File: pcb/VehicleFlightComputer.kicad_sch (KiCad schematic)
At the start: 52 parts, among them J3 USB_C_Receptacle, J4 Debug, Q1 S8050, SW1 B3U-1000P, U1 STM32H533VET6, U2 LIS2MDL, U3 LSM6DSV32X, U4 MCP2221A-I/ST, U5 AP2112K-3.3

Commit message: Added vehicle PDS I/O connector to `VehicleFlightComputer`.
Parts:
- added J1: FFC2B28-24-G, pcb:Flat Flexible Cable 24-Pin 0.5mm Connector, symbol Connector_Generic:Conn_01x22
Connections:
- net +3.3V: now also J1.12 (Pin_12), J1.18 (Pin_18), J1.5 (Pin_5)
- net GND: now also J1.1 (Pin_1), J1.11 (Pin_11), J1.13 (Pin_13), J1.15 (Pin_15), J1.22 (Pin_22), J1.9 (Pin_9)
- net sd_cmd: no longer names the net of U1.83 (PD2)
- net sd_data_0: no longer names the net of U1.65 (PC8)
- net sd_data_1: no longer names the net of U1.66 (PC9)
- net sd_data_2: no longer names the net of U1.78 (PC10)
- net sd_data_3: no longer names the net of U1.79 (PC11)
- new net +5V: J1.10 (Pin_10), J1.14 (Pin_14)
- new net BATTERY_ALLOWED: J1.17 (Pin_17)
- new net EXTERNAL_DETECTED: J1.16 (Pin_16)
- new net MOTOR_DIR_X: J1.21 (Pin_21)
- new net MOTOR_DIR_Y: J1.20 (Pin_20)
- new net MOTOR_DIR_Z: J1.19 (Pin_19)
- new net MOTOR_DISABLE: J1.6 (Pin_6)
- new net MOTOR_STEP_X: J1.2 (Pin_2)
- new net MOTOR_STEP_Y: J1.3 (Pin_3)
- new net MOTOR_STEP_Z: J1.4 (Pin_4)
- new net MOTOR_UART_RX: J1.7 (Pin_7)
- new net MOTOR_UART_TX: J1.8 (Pin_8)
- no-connect marks 135 -> 140
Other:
- removed sheet uSD Connector
- note added: "Pin ordering should account for backwards connection."
- note added: "Vehicle PDS I/O (V0)."
- moved on the sheet: BZ1, BZ2, C1, C10, C11, C12, C13, C15, C2, C3, C4, C5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

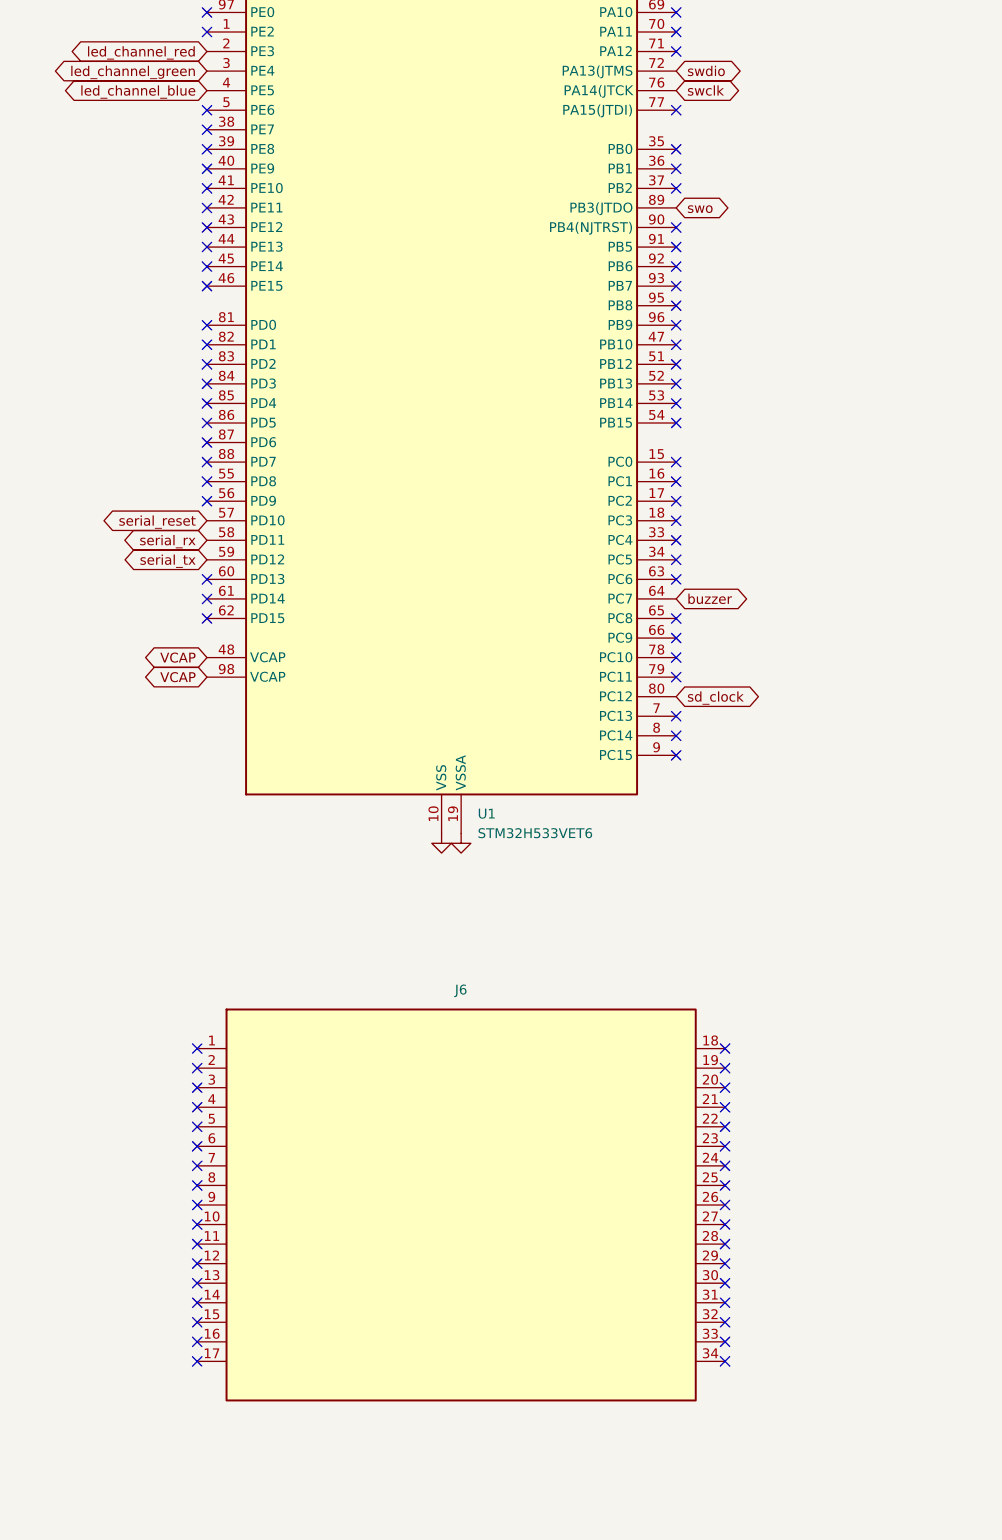
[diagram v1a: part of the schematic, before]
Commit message: Updated `VehicleStackConnector` with pin usages.
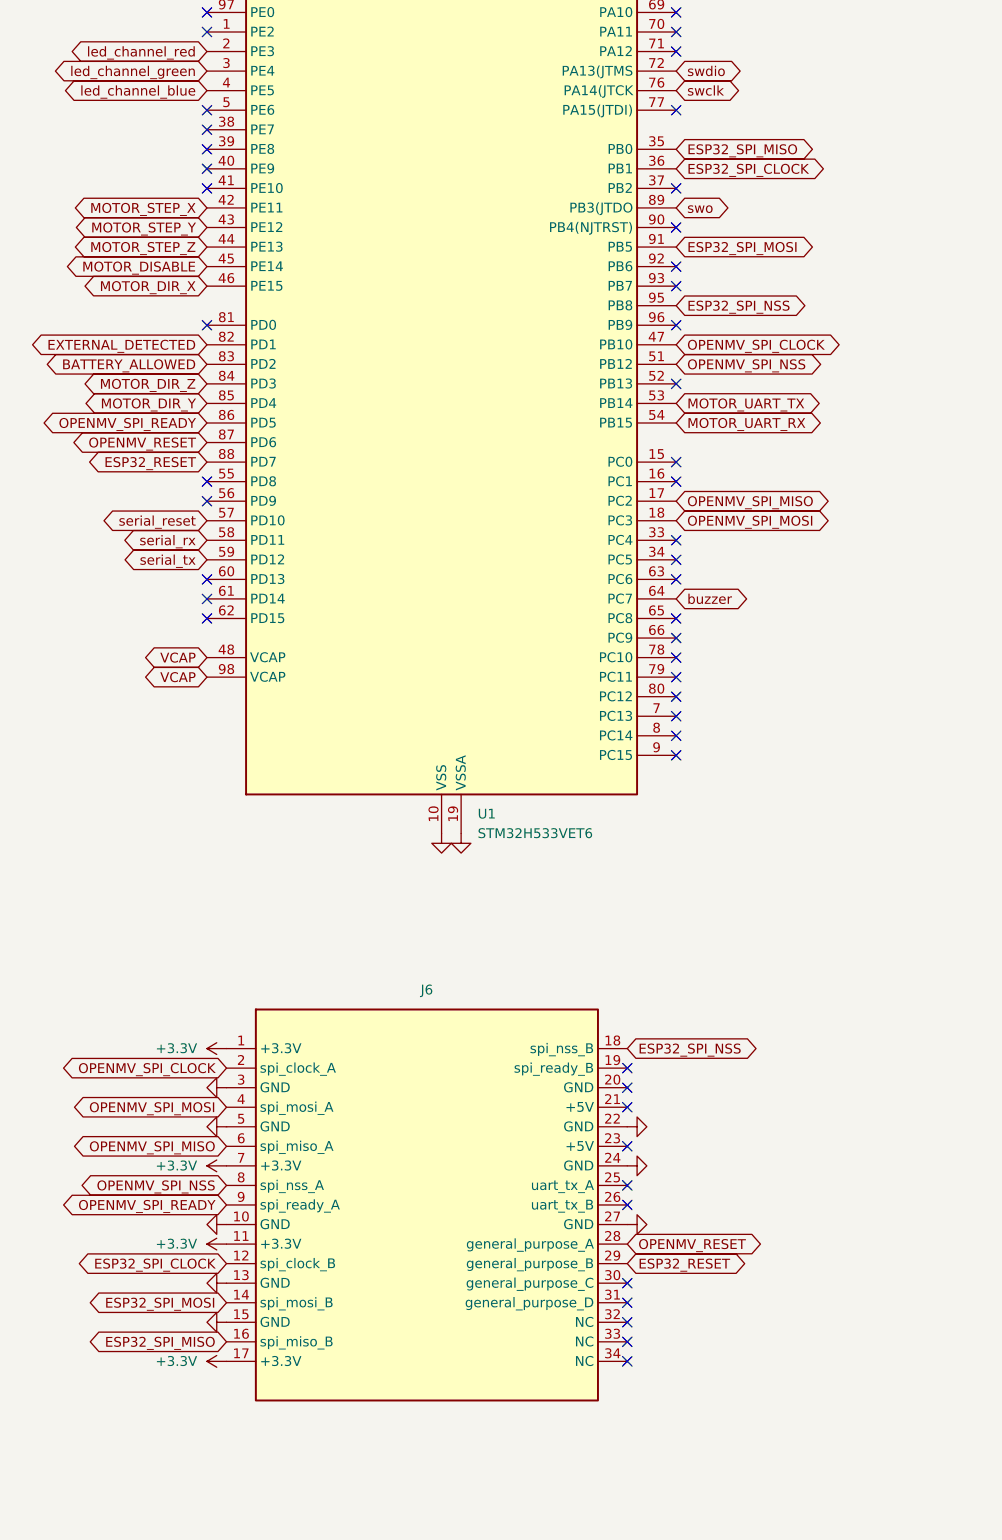
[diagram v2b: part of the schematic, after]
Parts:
- Q1: footprint Package_TO_SOT_SMD:SOT-23_Handsoldering -> Package_TO_SOT_THT:TO-92_Inline
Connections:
- net +3.3V: now also J6.1 (+3.3V), J6.11 (+3.3V), J6.17 (+3.3V), J6.7 (+3.3V)
- net BATTERY_ALLOWED: now also U1.83 (PD2)
- net EXTERNAL_DETECTED: now also U1.82 (PD1)
- net GND: now also J6.10 (GND), J6.13 (GND), J6.15 (GND), J6.22 (GND), J6.24 (GND), J6.27 (GND), J6.3 (GND), J6.5 (GND)
- net MOTOR_DIR_X: now also U1.46 (PE15)
- net MOTOR_DIR_Y: now also U1.85 (PD4)
- net MOTOR_DIR_Z: now also U1.84 (PD3)
- net MOTOR_DISABLE: now also U1.45 (PE14)
- net MOTOR_STEP_X: now also U1.42 (PE11)
- net MOTOR_STEP_Y: now also U1.43 (PE12)
- net MOTOR_STEP_Z: now also U1.44 (PE13)
- net MOTOR_UART_RX: now also U1.54 (PB15)
- net MOTOR_UART_TX: now also U1.53 (PB14)
- net ESP32_SPI_CLOCK: now reaches J6.12 (spi_clock_B)
- net ESP32_SPI_CLOCK: now also U1.36 (PB1)
- net ESP32_SPI_MOSI: now reaches J6.14 (spi_mosi_B)
- net ESP32_SPI_MOSI: now also U1.91 (PB5)
- net ESP32_SPI_MISO: now reaches J6.16 (spi_miso_B)
- net ESP32_SPI_MISO: now also U1.35 (PB0)
- net ESP32_SPI_NSS: now reaches J6.18 (spi_nss_B)
- net ESP32_SPI_NSS: now also U1.95 (PB8)
- net OPENMV_SPI_CLOCK: now reaches J6.2 (spi_clock_A)
- net OPENMV_SPI_CLOCK: now also U1.47 (PB10)
- net OPENMV_RESET: now reaches J6.28 (general_purpose_A)
- net OPENMV_RESET: now also U1.87 (PD6)
- net ESP32_RESET: now reaches J6.29 (general_purpose_B)
- net ESP32_RESET: now also U1.88 (PD7)
- net OPENMV_SPI_MOSI: now reaches J6.4 (spi_mosi_A)
- net OPENMV_SPI_MOSI: now also U1.18 (PC3)
- net OPENMV_SPI_MISO: now reaches J6.6 (spi_miso_A)
- net OPENMV_SPI_MISO: now also U1.17 (PC2)
- net OPENMV_SPI_NSS: now reaches J6.8 (spi_nss_A)
- net OPENMV_SPI_NSS: now also U1.51 (PB12)
- net OPENMV_SPI_READY: now reaches J6.9 (spi_ready_A)
- net OPENMV_SPI_READY: now also U1.86 (PD5)
- net sd_clock: no longer names the net of U1.80 (PC12)
- no-connect marks 140 -> 96

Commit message: `Debug Buzzer (V5 : AST only).`
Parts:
- removed BZ2: WT-1205, Buzzer_Beeper:MagneticBuzzer_ProSignal_ABT-410-RC, symbol Device:Buzzer
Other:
- note added: "Debug Buzzer (V5 : AST only)."
- note removed: "Debug Buzzer (V4 : Transistor)."
- note removed: "TODO: The AST1109MLTRQ and WT-1205 buzzers have similar footprint area, but the former has a much smaller height. As precaution, we'll have a footprint for both buzzers in case we design for the AST1109MLTRQ wrong."
- moved on the sheet: BZ1, C1, C10, C2, C3, C4, C5, C6, C8, C9, H1, H2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

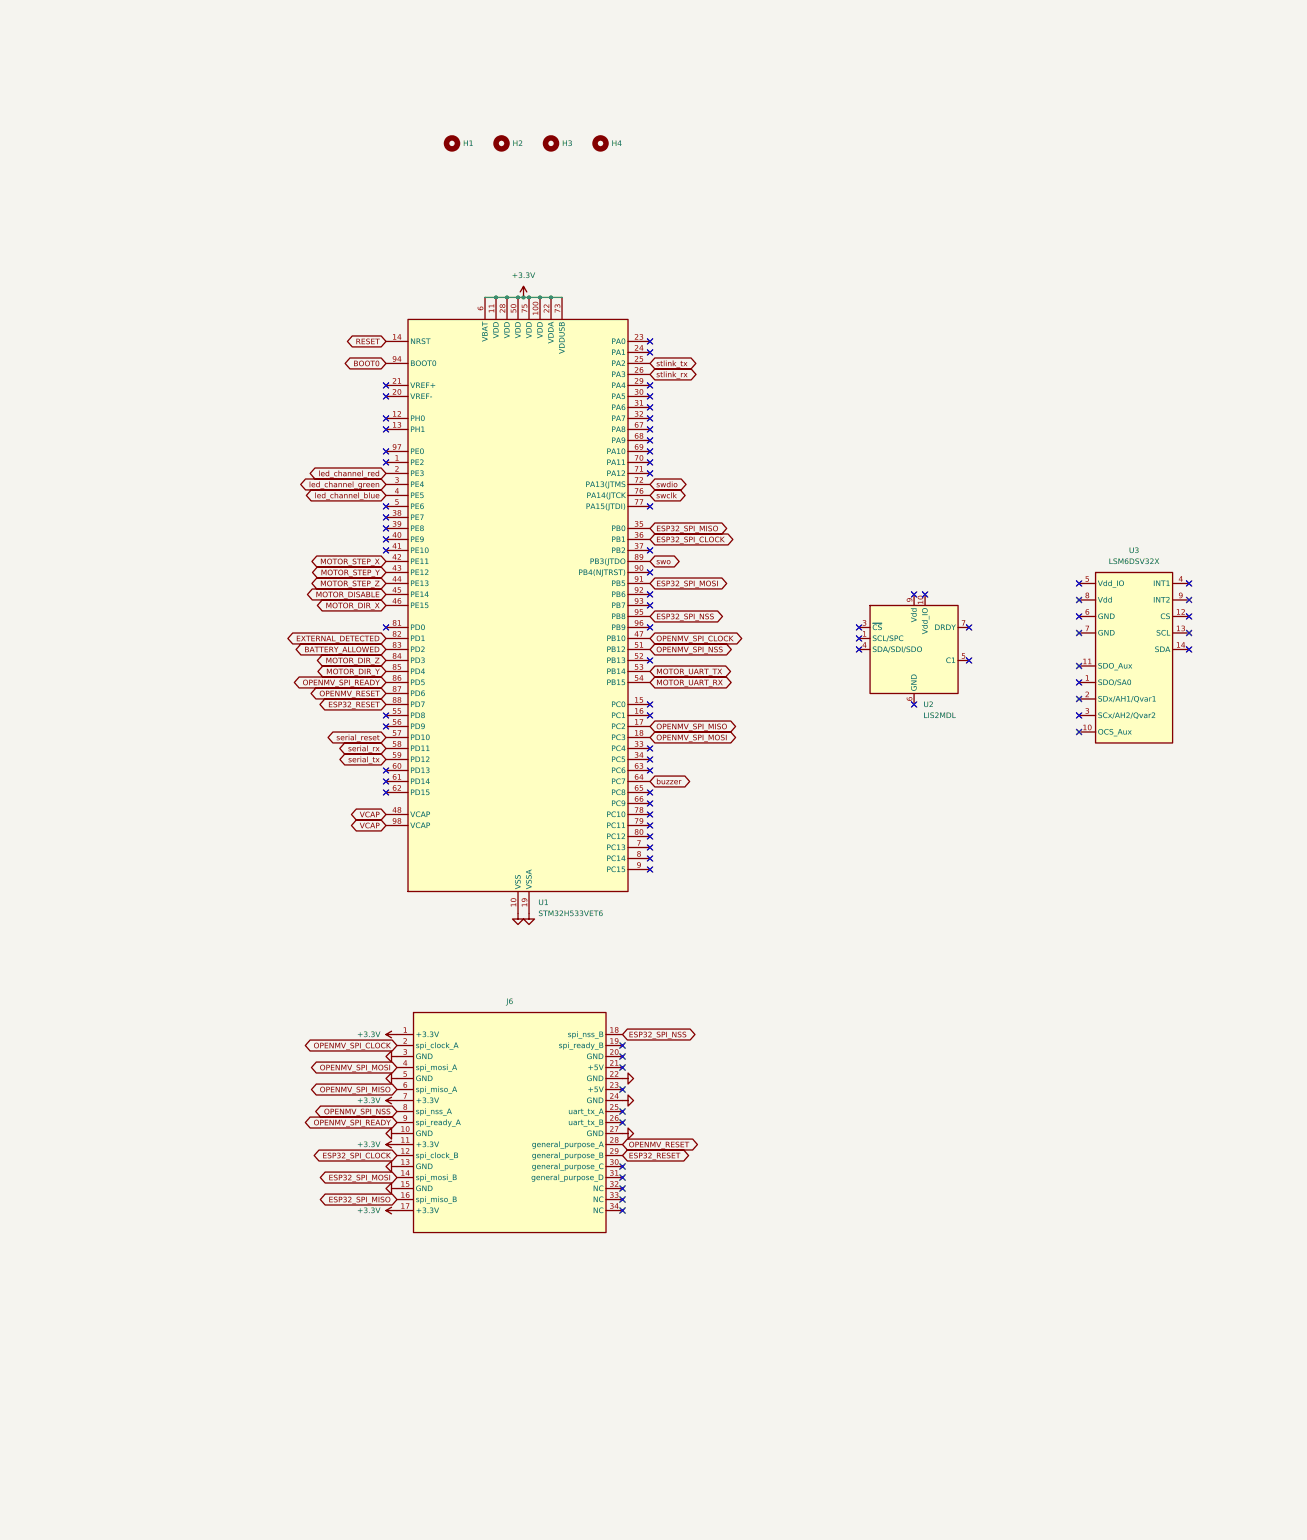
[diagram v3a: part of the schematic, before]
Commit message: Set up schematic for LSM6DSV32X on `VehicleFlightComputer`.
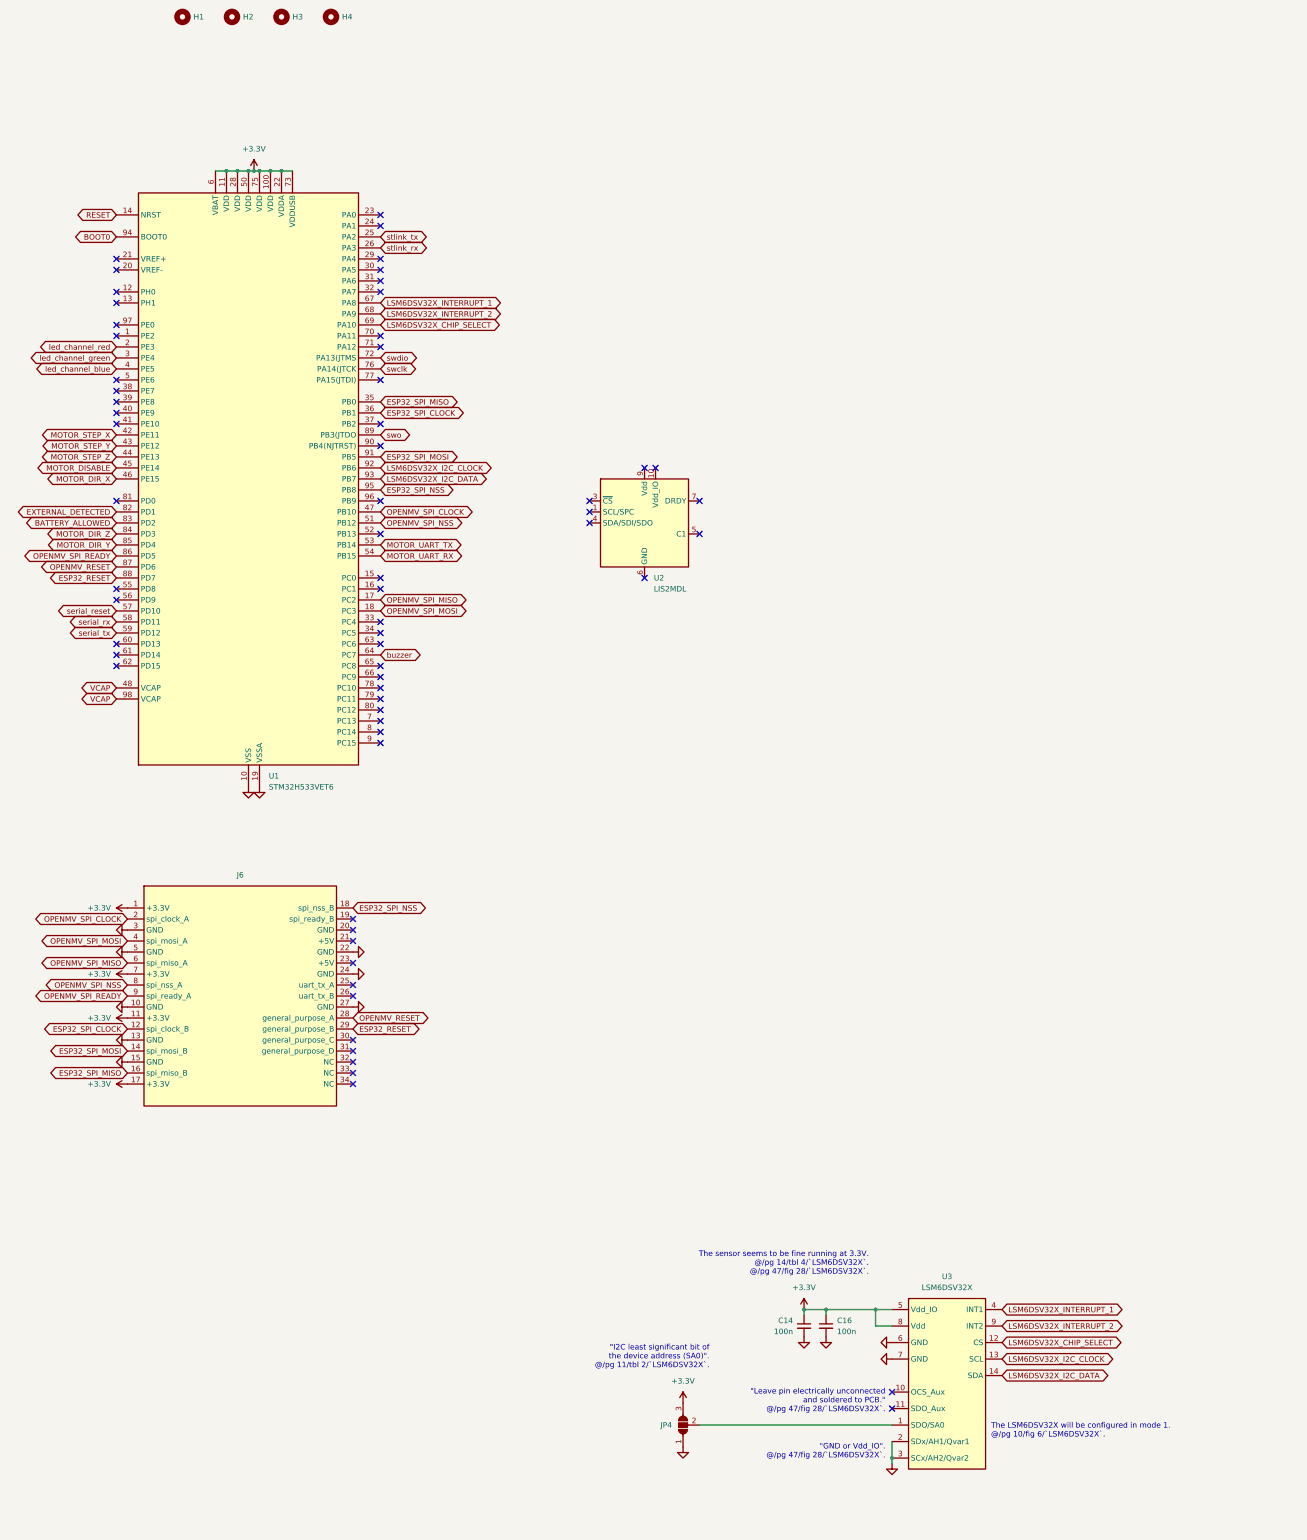
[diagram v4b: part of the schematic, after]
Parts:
- added C14, C16: 100n, Capacitor_SMD:C_1206_3216Metric_Pad1.33x1.80mm_HandSolder, symbol Device:C_Small
- added JP4: SolderJumper_3_Open, symbol Jumper:SolderJumper_3_Open
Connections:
- net +3.3V: now also U3.5 (Vdd_IO), U3.8 (Vdd), C14.1, C16.1, JP4.3 (B)
- net GND: now also U3.2 (SDx/AH1/Qvar1), U3.3 (SCx/AH2/Qvar2), U3.6 (GND), U3.7 (GND), C14.2, C16.2, JP4.1 (A)
- net at U3.1 (SDO/SA0): now also JP4.2 (C)
- net LSM6DSV32X_CHIP_SELECT: now reaches U3.12 (CS)
- net LSM6DSV32X_CHIP_SELECT: now also U1.69 (PA10)
- net LSM6DSV32X_I2C_CLOCK: now reaches U3.13 (SCL)
- net LSM6DSV32X_I2C_CLOCK: now also U1.92 (PB6)
- net LSM6DSV32X_I2C_DATA: now reaches U3.14 (SDA)
- net LSM6DSV32X_I2C_DATA: now also U1.93 (PB7)
- net LSM6DSV32X_INTERRUPT_1: now reaches U3.4 (INT1)
- net LSM6DSV32X_INTERRUPT_1: now also U1.67 (PA8)
- net LSM6DSV32X_INTERRUPT_2: now reaches U3.9 (INT2)
- net LSM6DSV32X_INTERRUPT_2: now also U1.68 (PA9)
- no-connect marks 96 -> 79
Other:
- note added: ""GND or Vdd_IO". @/pg 47/fig 28/`LSM6DSV32X`."
- note added: ""I2C least significant bit of the device address (SA0)". @/pg 11/tbl 2/`LSM6DSV32X`."
- note added: ""Leave pin electrically unconnected and soldered to PCB." @/pg 47/fig 28/`LSM6DSV32X`."
- note added: "The LSM6DSV32X will be configured in mode 1. @/pg 10/fig 6/`LSM6DSV32X`."
- note added: "The sensor seems to be fine running at 3.3V. @/pg 14/tbl 4/`LSM6DSV32X`. @/pg 47/fig 28/`LSM6DSV32X`."
- moved on the sheet: H1, H2, H3, H4, J6, U1, U2, U3
